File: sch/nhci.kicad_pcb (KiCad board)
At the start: 4 copper layers, 67 parts, among them IC1 74LVC8T245RHLRG4, IC2 74LVC8T245RHLRG4, IC3 74LVC8T245RHLRG4, IC4 74LVC8T245RHLRG4, IC5 74LVC8T245RHLRG4, IC6 MAX3421EEHJ+, IC7 LT3030IFE#TRPBF, J1 CLP-105-02-F-D, SW1 SW_Push_Open, U1 PCMCIA_BOARD, U2 iCE40-HX8K-CT256, U3 N25Q032A13EF440F, U4 LM3526M-H, Y1 ECS-5032MV-120-BM-TR

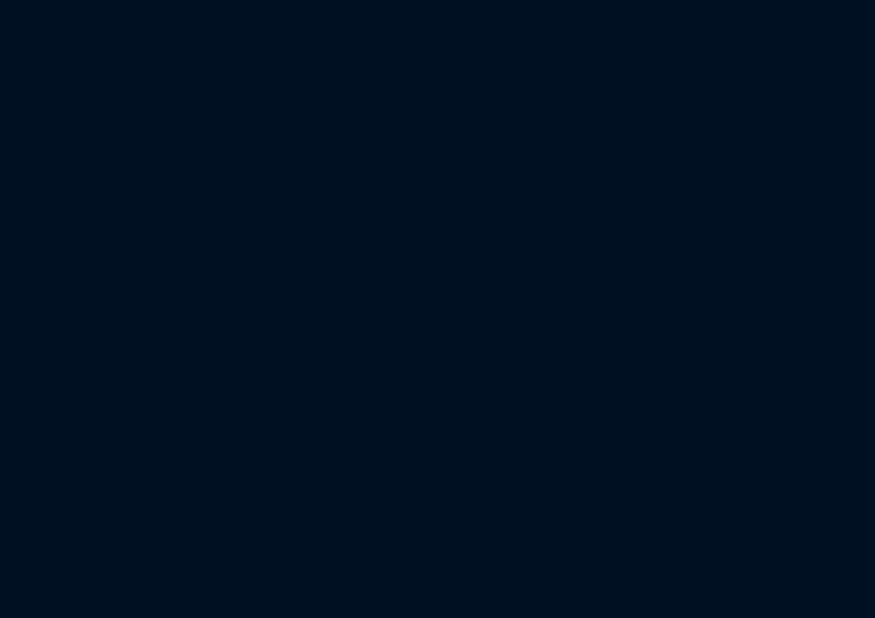
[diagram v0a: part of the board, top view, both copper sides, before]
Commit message: Add power led
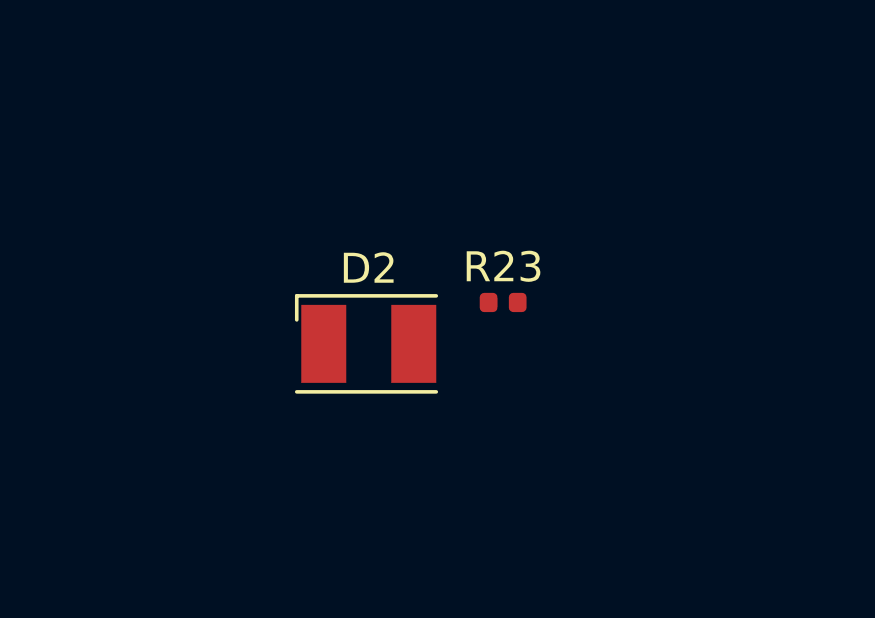
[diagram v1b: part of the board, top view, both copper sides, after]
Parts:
- added D2: LED, LED_SMD:LED_PLCC-2, F.Cu at (52.6, 174.5)
- added R23: 1k, Resistor_SMD:R_0402_1005Metric, F.Cu at (57.1, 173.1)
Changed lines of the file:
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@@
     (tracks 1111)
     (zones 0)
-    (modules 67)
-    (nets 356)
+    (modules 69)
+    (nets 357)
   )
   (page A4)
@@
   (net 354 CRESET)
   (net 355 CDONE)
+  (net 356 "Net-(D2-Pad2)")
   (net_class Default "This is the default net class."
     (clearance 0.127)
@@
     (add_net "Net-(C29-Pad1)")
     (add_net "Net-(D1-Pad1)")
+    (add_net "Net-(D2-Pad2)")
     (add_net "Net-(IC1-PadEP1)")
     (add_net "Net-(IC1-PadEP2)")
@@
   )
   (module Resistor_SMD:R_0402_1005Metric (layer F.Cu)
+    (at 57.058 173.118)
+    (descr "Resistor SMD 0402 (1005 Metric), square (rectangular) end terminal, IPC_7351 nominal, (Body size source: http://www.tortai-tech.com/upload/download/2011102023233369053.pdf), generated with kicad-footprint-generator")
+    (tags resistor)
+    (attr smd)
+    (fp_text reference R23 (at 0 -1.17) (layer F.SilkS)
+      (effects (font (size 1 1) (thickness 0.15)))
+    )
+    (fp_text value 1k (at 0 1.17) (layer F.Fab)
+      (effects (font (size 1 1) (thickness 0.15)))
+    )
+    (fp_text user %R (at 0 0) (layer F.Fab)
+      (effects (font (size 0.25 0.25) (thickness 0.04)))
+    )
+    (fp_line (start -0.5 0.25) (end -0.5 -0.25) (layer F.Fab) (width 0.1))
+    (fp_line (start -0.5 -0.25) (end 0.5 -0.25) (layer F.Fab) (width 0.1))
+    (fp_line (start 0.5 -0.25) (end 0.5 0.25) (layer F.Fab) (width 0.1))
+    (fp_line (start 0.5 0.25) (end -0.5 0.25) (layer F.Fab) (width 0.1))
+    (fp_line (start -0.93 0.47) (end -0.93 -0.47) (layer F.CrtYd) (width 0.05))
+    (fp_line (start -0.93 -0.47) (end 0.93 -0.47) (layer F.CrtYd) (width 0.05))
+    (fp_line (start 0.93 -0.47) (end 0.93 0.47) (layer F.CrtYd) (width 0.05))
+    (fp_line (start 0.93 0.47) (end -0.93 0.47) (layer F.CrtYd) (width 0.05))
+    (pad 2 smd roundrect (at 0.485 0) (size 0.59 0.64) (layers F.Cu F.Paste F.Mask) (roundrect_rratio 0.25)
+      (net 356 "Net-(D2-Pad2)"))
+    (pad 1 smd roundrect (at -0.485 0) (size 0.59 0.64) (layers F.Cu F.Paste F.Mask) (roundrect_rratio 0.25)
+      (net 336 "Net-(C29-Pad1)"))
+    (model ${KISYS3DMOD}/Resistor_SMD.3dshapes/R_0402_1005Metric.wrl
+      (at (xyz 0 0 0))
+      (scale (xyz 1 1 1))
+      (rotate (xyz 0 0 0))
+    )
+  )
+  (module LED_SMD:LED_PLCC-2 (layer F.Cu)
+    (at 52.578 174.498)
+    (descr "LED PLCC-2 SMD package")
+    (tags "LED PLCC-2 SMD")
+    (attr smd)
+    (fp_text reference D2 (at 0 -2.5) (layer F.SilkS)
+      (effects (font (size 1 1) (thickness 0.15)))
+    )
+    (fp_text value LED (at 0 2.5) (layer F.Fab)
+      (effects (font (size 1 1) (thickness 0.15)))
+    )
+    (fp_text user %R (at 0 0) (layer F.Fab)
+      (effects (font (size 0.4 0.4) (thickness 0.1)))
+    )
+    (fp_circle (center 0 0) (end 0 -1.25) (layer F.Fab) (width 0.1))
+    (fp_line (start -1.7 -0.6) (end -0.8 -1.5) (layer F.Fab) (width 0.1))
+    (fp_line (start 1.7 1.5) (end 1.7 -1.5) (layer F.Fab) (width 0.1))
+    (fp_line (start 1.7 -1.5) (end -1.7 -1.5) (layer F.Fab) (width 0.1))
+    (fp_line (start -1.7 -1.5) (end -1.7 1.5) (layer F.Fab) (width 0.1))
+    (fp_line (start -1.7 1.5) (end 1.7 1.5) (layer F.Fab) (width 0.1))
+    (fp_line (start -2.65 -1.85) (end 2.5 -1.85) (layer F.CrtYd) (width 0.05))
+    (fp_line (start 2.5 -1.85) (end 2.5 1.85) (layer F.CrtYd) (width 0.05))
+    (fp_line (start 2.5 1.85) (end -2.65 1.85) (layer F.CrtYd) (width 0.05))
+    (fp_line (start -2.65 1.85) (end -2.65 -1.85) (layer F.CrtYd) (width 0.05))
+    (fp_line (start 2.25 1.6) (end -2.4 1.6) (layer F.SilkS) (width 0.12))
+    (fp_line (start 2.25 -1.6) (end -2.4 -1.6) (layer F.SilkS) (width 0.12))
+    (fp_line (start -2.4 -1.6) (end -2.4 -0.8) (layer F.SilkS) (width 0.12))
+    (pad 2 smd rect (at 1.5 0) (size 1.5 2.6) (layers F.Cu F.Paste F.Mask)
+      (net 356 "Net-(D2-Pad2)"))
+    (pad 1 smd rect (at -1.5 0) (size 1.5 2.6) (layers F.Cu F.Paste F.Mask)
+      (net 69 GND))
+    (model ${KISYS3DMOD}/LED_SMD.3dshapes/LED_PLCC-2.wrl
+      (at (xyz 0 0 0))
+      (scale (xyz 1 1 1))
+      (rotate (xyz 0 0 0))
+    )
+  )
+  (module Resistor_SMD:R_0402_1005Metric (layer F.Cu)

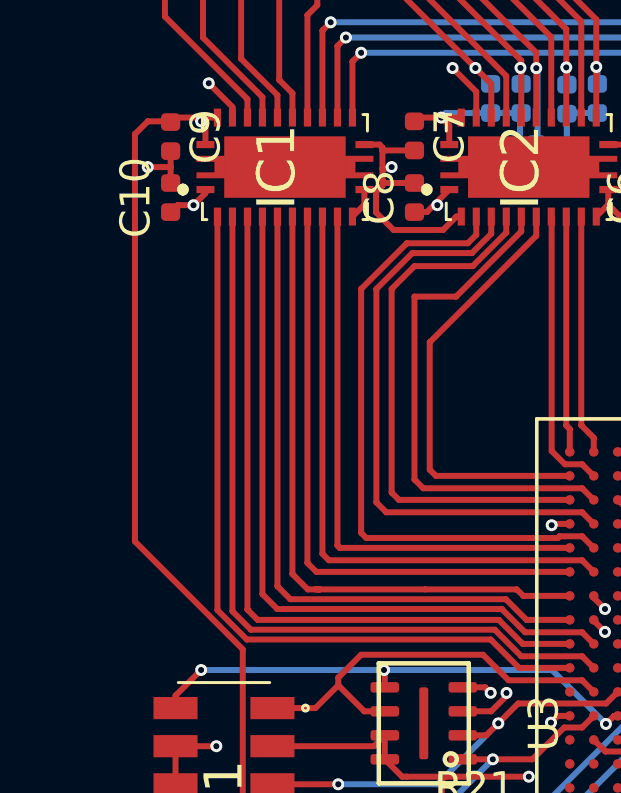
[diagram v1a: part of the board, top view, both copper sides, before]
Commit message: Add pulldown resistor so when FPGA boots no load on data bus
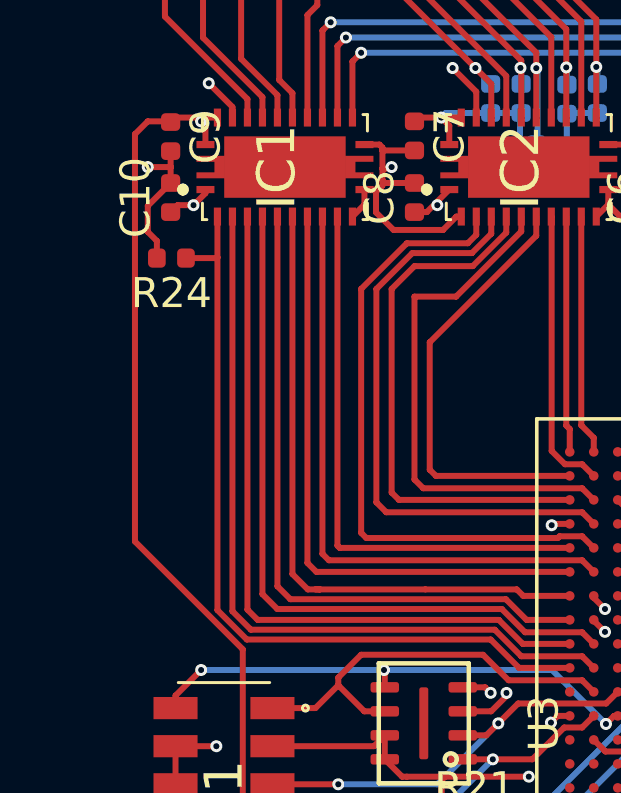
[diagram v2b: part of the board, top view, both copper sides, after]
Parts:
- added R24: 10k, Resistor_SMD:R_0402_1005Metric, F.Cu at (46.0, 112.0)
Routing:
- net GND: track 142.4 -> 145.3 mm
- net F_DDIR: track 25.7 -> 26.7 mm

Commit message: Add Connector
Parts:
- removed R24: 10k, Resistor_SMD:R_0402_1005Metric
- D2: footprint LED_SMD:LED_PLCC-2 -> LED_SMD:LED_0603_1608Metric
- moved D2 3.99 mm to (55.7, 177.0)
- moved R23 2.64 mm to (58.2, 175.5), turned to 270 degrees
- moved SW1 1.07 mm to (75.4, 180.1)
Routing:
- net Net-(C29-Pad1): track 9.40 -> 61.5 mm, vias 0 -> 2
- net GND: track 145.3 -> 174.9 mm, vias 38 -> 42
- net Net-(R19-Pad1): track 0.00 -> 27.2 mm, vias 0 -> 2
- net Net-(JP1-Pad2): track 103.8 -> 127.5 mm
- net Net-(R20-Pad1): track 0.00 -> 23.5 mm, vias 0 -> 1
- net Net-(D2-Pad2): track 0.00 -> 2.16 mm
- net F_DDIR: track 26.7 -> 25.7 mm

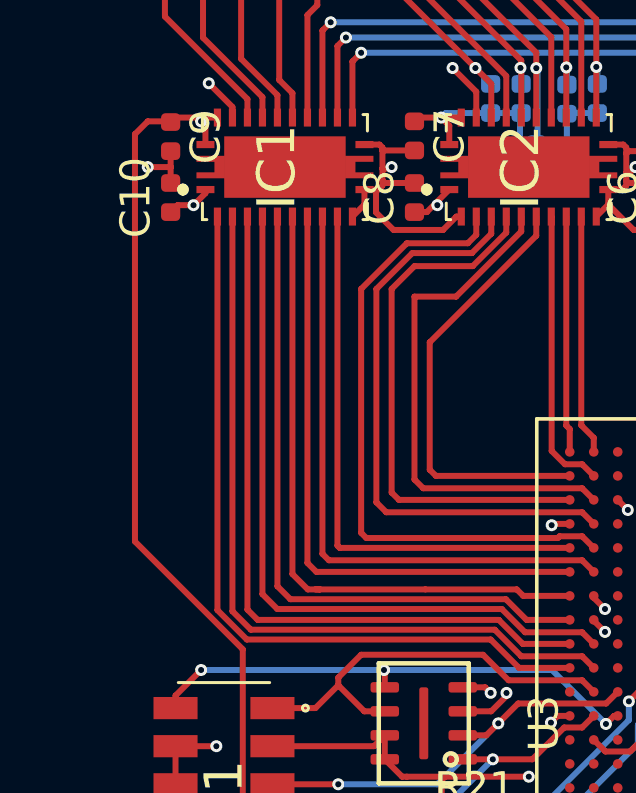
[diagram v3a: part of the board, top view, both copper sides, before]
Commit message: Add eaten resistor (move between machines)
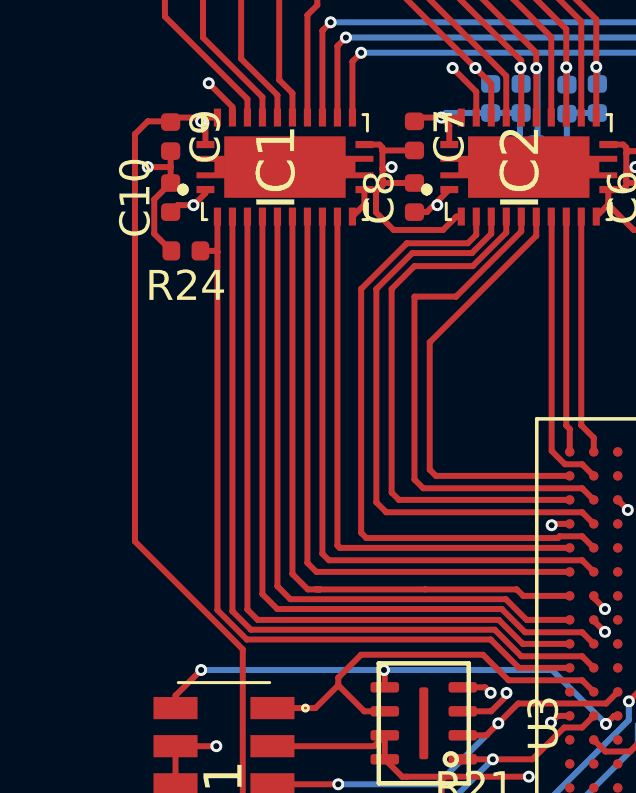
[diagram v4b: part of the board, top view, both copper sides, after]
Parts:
- added R24: 10k, Resistor_SMD:R_0402_1005Metric, F.Cu at (46.5, 111.8)
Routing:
- net GND: track 174.9 -> 177.6 mm
- net F_DDIR: track 25.7 -> 26.2 mm
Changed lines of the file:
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@@
     (thickness 1.6)
     (drawings 0)
-    (tracks 1181)
+    (tracks 1187)
     (zones 0)
-    (modules 69)
+    (modules 70)
     (nets 369)
   )
@@
     (add_net U_SS)
   )
+  (module Resistor_SMD:R_0402_1005Metric (layer F.Cu)
+    (at 46.482 111.76 180)
+    (descr "Resistor SMD 0402 (1005 Metric), square (rectangular) end terminal, IPC_7351 nominal, (Body size source: http://www.tortai-tech.com/upload/download/2011102023233369053.pdf), generated with kicad-footprint-generator")
+    (tags resistor)
+    (attr smd)
+    (fp_text reference R24 (at 0 -1.17) (layer F.SilkS)
+      (effects (font (size 1 1) (thickness 0.15)))
+    )
+    (fp_text value 10k (at 0 1.17) (layer F.Fab)
+      (effects (font (size 1 1) (thickness 0.15)))
+    )
+    (fp_text user %R (at 0 0) (layer F.Fab)
+      (effects (font (size 0.25 0.25) (thickness 0.04)))
+    )
+    (fp_line (start -0.5 0.25) (end -0.5 -0.25) (layer F.Fab) (width 0.1))
+    (fp_line (start -0.5 -0.25) (end 0.5 -0.25) (layer F.Fab) (width 0.1))
+    (fp_line (start 0.5 -0.25) (end 0.5 0.25) (layer F.Fab) (width 0.1))
+    (fp_line (start 0.5 0.25) (end -0.5 0.25) (layer F.Fab) (width 0.1))
+    (fp_line (start -0.93 0.47) (end -0.93 -0.47) (layer F.CrtYd) (width 0.05))
+    (fp_line (start -0.93 -0.47) (end 0.93 -0.47) (layer F.CrtYd) (width 0.05))
+    (fp_line (start 0.93 -0.47) (end 0.93 0.47) (layer F.CrtYd) (width 0.05))
+    (fp_line (start 0.93 0.47) (end -0.93 0.47) (layer F.CrtYd) (width 0.05))
+    (pad 2 smd roundrect (at 0.485 0 180) (size 0.59 0.64) (layers F.Cu F.Paste F.Mask) (roundrect_rratio 0.25)
+      (net 69 GND))
+    (pad 1 smd roundrect (at -0.485 0 180) (size 0.59 0.64) (layers F.Cu F.Paste F.Mask) (roundrect_rratio 0.25)
+      (net 277 F_DDIR))
+    (model ${KISYS3DMOD}/Resistor_SMD.3dshapes/R_0402_1005Metric.wrl
+      (at (xyz 0 0 0))
+      (scale (xyz 1 1 1))
+      (rotate (xyz 0 0 0))
+    )
+  )
   (module own:PCMCIA_CARD locked (layer F.Cu)
     (at 65.786 97.282)
@@
   (via (at 54.864 167.386) (size 0.8) (drill 0.4) (layers F.Cu B.Cu) (net 69))
   (segment (start 54.864 177.038) (end 54.864 167.386) (width 0.2) (layer F.Cu) (net 69))
+  (segment (start 45.42699 110.04401) (end 45.974 109.497) (width 0.2) (layer F.Cu) (net 69))
+  (segment (start 45.42699 111.18999) (end 45.42699 110.04401) (width 0.2) (layer F.Cu) (net 69))
+  (segment (start 45.997 111.76) (end 45.42699 111.18999) (width 0.2) (layer F.Cu) (net 69))
   (segment (start 49.034 106.634302) (end 49.034 107.316) (width 0.2) (layer F.Cu) (net 70))
   (segment (start 47.0535 104.653802) (end 49.034 106.634302) (width 0.2) (layer F.Cu) (net 70))
@@
   (segment (start 57.588 125.66) (end 56.642 124.714) (width 0.2) (layer F.Cu) (net 277))
   (segment (start 56.642 124.714) (end 48.514 124.714) (width 0.2) (layer F.Cu) (net 277))
-  (segment (start 47.534 123.734) (end 47.534 110.616) (width 0.2) (layer F.Cu) (net 277))
   (segment (start 48.514 124.714) (end 47.534 123.734) (width 0.2) (layer F.Cu) (net 277))
+  (segment (start 46.967 111.76) (end 47.498 111.76) (width 0.2) (layer F.Cu) (net 277))
+  (segment (start 47.498 111.76) (end 47.534 111.796) (width 0.2) (layer F.Cu) (net 277))
+  (segment (start 47.534 123.734) (end 47.534 111.796) (width 0.2) (layer F.Cu) (net 277))
+  (segment (start 47.534 111.796) (end 47.534 110.616) (width 0.2) (layer F.Cu) (net 277))
   (segment (start 59.278 123.26) (end 57.728 123.26) (width 0.2) (layer F.Cu) (net 278))
   (segment (start 57.728 123.26) (end 57.51198 123.04398) (width 0.2) (layer F.Cu) (net 278))

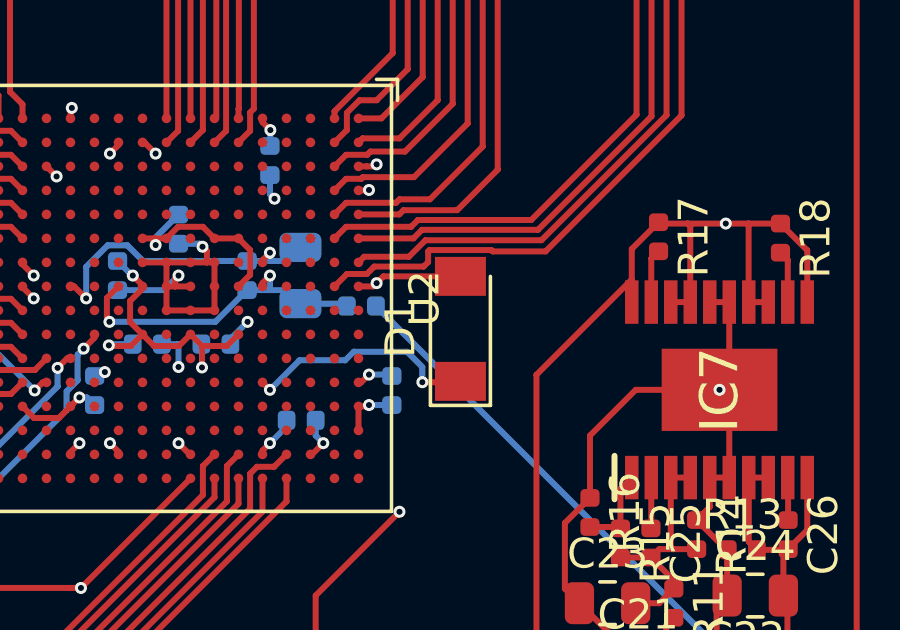
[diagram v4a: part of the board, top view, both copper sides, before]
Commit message: Replace diode
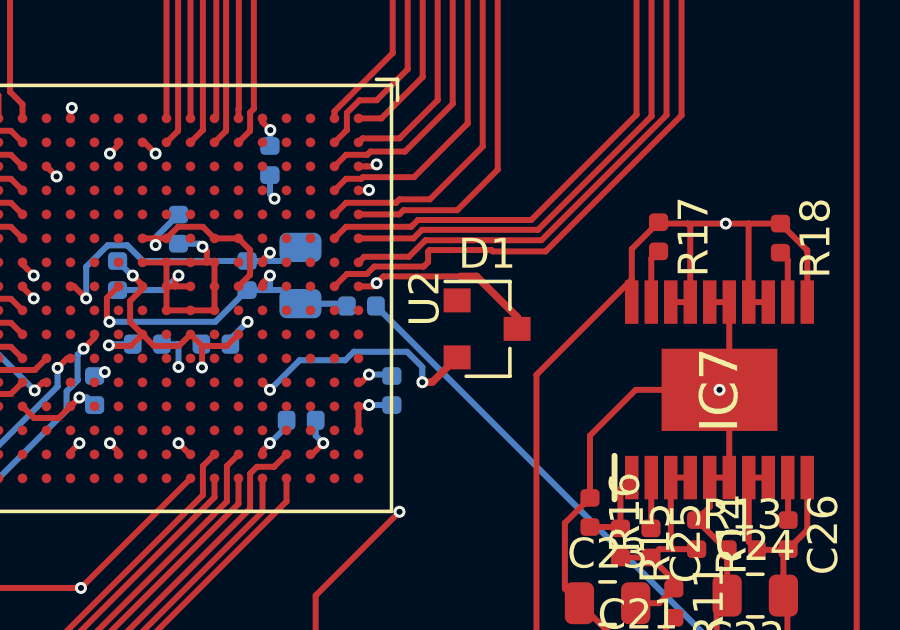
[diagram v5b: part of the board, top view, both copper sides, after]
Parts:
- D1: value LL4148 -> BAT54S; footprint Diode_SMD:D_MiniMELF -> Package_TO_SOT_SMD:SOT-23
- moved D1 0.89 mm to (75.6, 125.5), turned to 0 degrees
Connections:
- D1 pad 2: +3V3 -> Net-(D1-Pad2)
- U2 pad E12: Net-(D1-Pad1) -> Net-(D1-Pad2)
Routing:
- net Net-(D1-Pad2): track 0.00 -> 8.18 mm, vias 0 -> 2
- net Net-(D1-Pad1): track 7.95 -> 0.00 mm, vias 2 -> 0
- net +3V3: track 134.4 -> 137.3 mm
